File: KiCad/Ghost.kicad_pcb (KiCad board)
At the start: 2 copper layers, 90.3 x 63 mm, 68 parts, among them P1 MOTOR, P2 SERVO, P3 START, P4 PWM, P5 RGB, Q1 MMBT3904, SW1 BTN1, U1 INA219, U10 GP2Y0E02B, U11 GP2Y0E02B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

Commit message: Started on Feature Tests in Arduino
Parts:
- removed the REF** at (111.3, 103.6)
- added REF**: 3mm_mounting_hole, NorBotKiCadFootprints:3mm_mounting_hole, F.Cu at (111.3, 103.6)
- added REF**: 3mm_mounting_hole, NorBotKiCadFootprints:3mm_mounting_hole, F.Cu at (181.0, 130.0)
- added REF**: 3mm_mounting_hole, NorBotKiCadFootprints:3mm_mounting_hole, F.Cu at (181.0, 74.7)
- added REF**: 3mm_mounting_hole, NorBotKiCadFootprints:3mm_mounting_hole, F.Cu at (163.6, 99.3)
- added REF**: 3mm_mounting_hole, NorBotKiCadFootprints:3mm_mounting_hole, F.Cu at (163.8, 108.6)
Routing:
- net /IRSensors/SD3: track 37.0 -> 39.7 mm
- net WIFI_RX: track 22.3 -> 24.1 mm
- net /IRSensors/SC3: track 39.5 -> 40.8 mm
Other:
- outline, holes or cut-outs redrawn

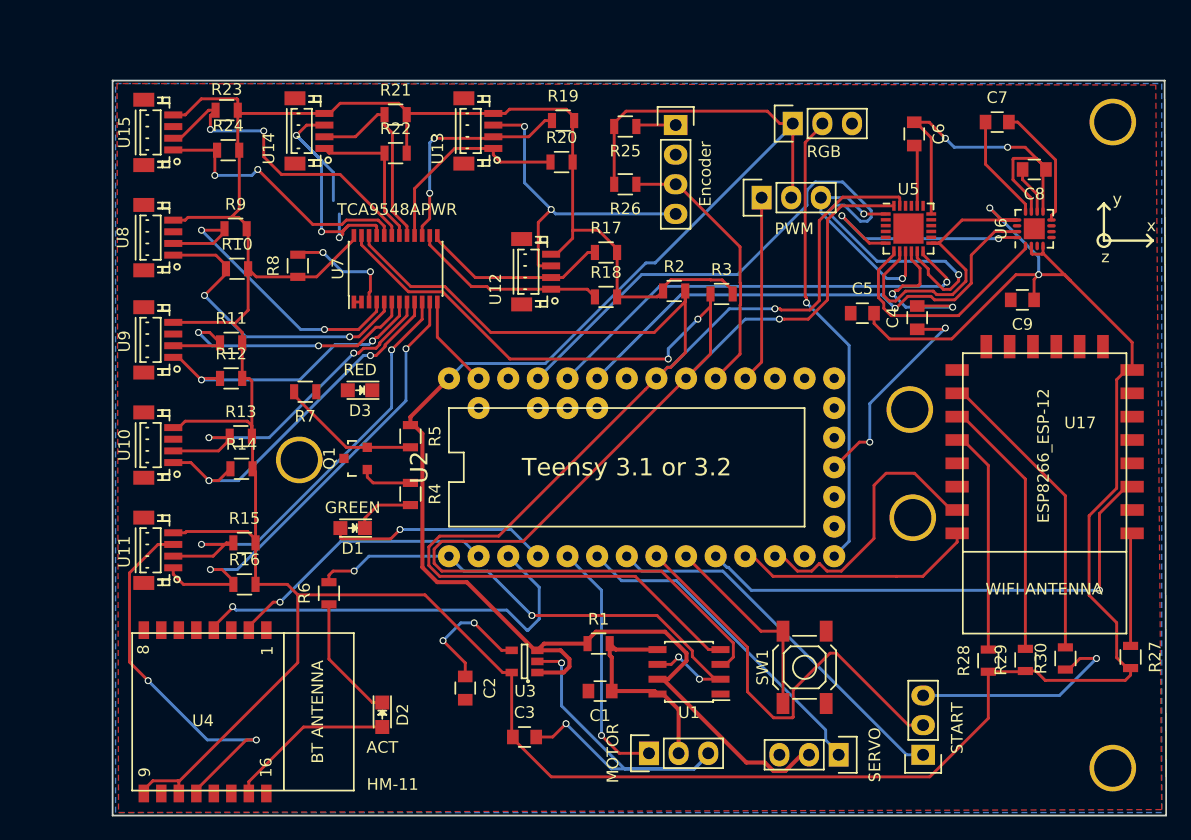
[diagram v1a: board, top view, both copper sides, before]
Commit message: Working on PCB layout for Rev 2
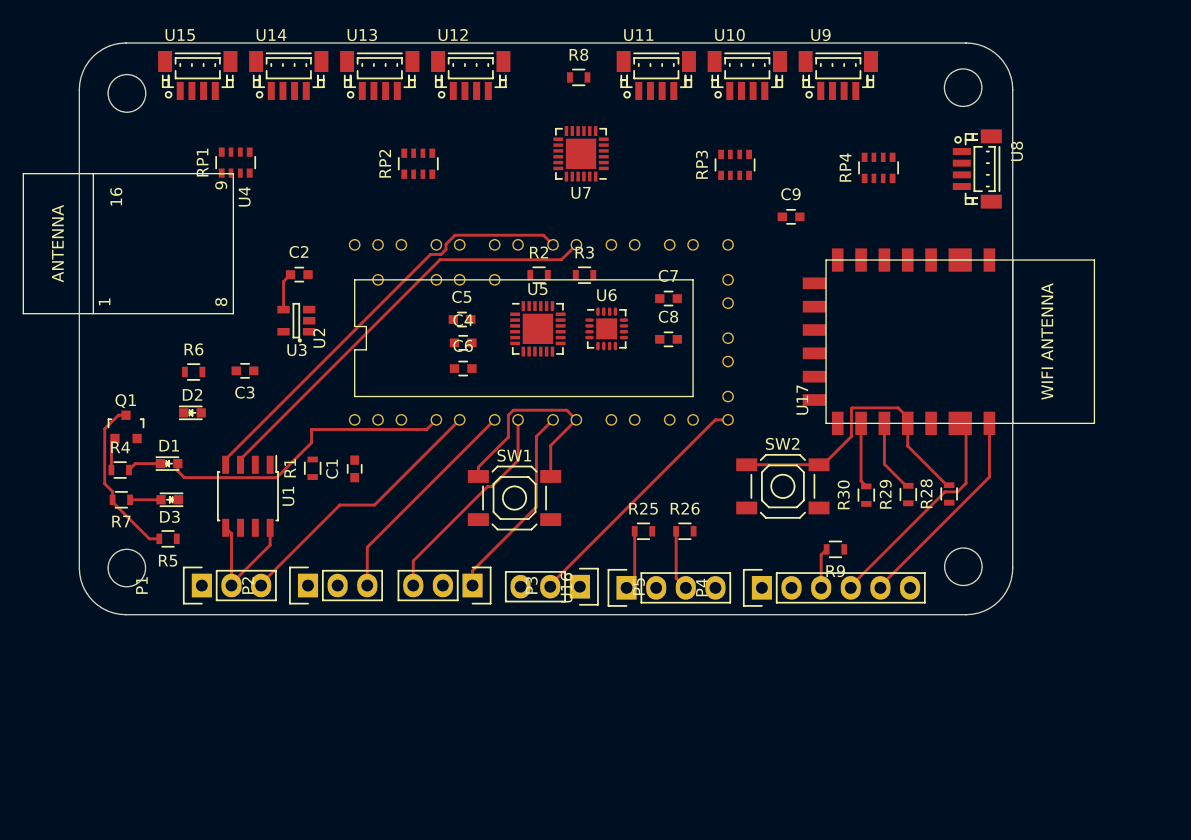
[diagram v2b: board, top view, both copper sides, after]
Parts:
- removed R10, R11, R12, R13, R14, R15, R16, R17, R18, R19, R20, R21, R22, R23, R24: 1k, Resistors_SMD:R_0805
- removed R27: 3k3, Resistors_SMD:R_0805
- removed REF**: Symbol_OSHW-Logo_SilkScreen, Symbols:Symbol_OSHW-Logo_SilkScreen
- removed REF** (x5): 3mm_mounting_hole, NorBotKiCadFootprints:3mm_mounting_hole
- added RP1: 4 x 1k ohm, Resistors_SMD:R_Array_Convex_4x0603, F.Cu at (105.8, 78.2)
- added RP2: 4 x 1k ohm, Resistors_SMD:R_Array_Convex_4x0603, F.Cu at (121.5, 78.2)
- added RP3: 4 x 1k ohm, Resistors_SMD:R_Array_Convex_4x0603, F.Cu at (148.6, 78.3)
- added RP4: 4 x 1k ohm, Resistors_SMD:R_Array_Convex_4x0603, F.Cu at (160.9, 78.6)
- added SW2: PROG, Buttons_Switches_SMD:SW_SPST_SKQG, F.Cu at (152.7, 105.9)
- C1, C2, C3, C4, C5, C6, C7, C8, C9: footprint Capacitors_SMD:C_0805 -> Capacitors_SMD:C_0603
- D1, D2, D3: footprint LEDs:LED_0805 -> LEDs:LED_0603
- P4: value PWM -> CONN_01X06; footprint Pin_Headers:Pin_Header_Straight_1x03 -> Pin_Headers:Pin_Header_Straight_1x06
- R1, R2, R25, R26, R28, R29, R3, R30, R4, R5, R6, R7, R8: footprint Resistors_SMD:R_0805 -> Resistors_SMD:R_0603
- R9: value 1k -> 0; footprint Resistors_SMD:R_0805 -> Resistors_SMD:R_0603
- U16: value Encoder -> Transmissive_Photo_Interrupter
- U2: value Teensy 3.1 or 3.2 -> Teensy31_32
- U7: value TCA9548APWR -> TCA9548ARGER; footprint Housings_SSOP:TSSOP-24_4.4x7.8mm_Pitch0.65mm -> Housings_DFN_QFN:QFN-24-1EP_4x4mm_Pitch0.5mm
- moved U8 70.4 mm to (169.3, 78.7), turned to 270 degrees
- moved U9 62.5 mm to (157.4, 70.8), turned to 0 degrees
- moved U10 59.5 mm to (149.7, 70.8), turned to 0 degrees
- moved U11 58.9 mm to (141.8, 70.8), turned to 0 degrees
- moved R9 58.3 mm to (157.2, 111.3), turned to 180 degrees
- moved P2 47.7 mm to (112.0, 114.4), turned to 90 degrees
- moved P5 43.7 mm to (135.3, 114.5), turned to 270 degrees
- moved C6 43.6 mm to (125.3, 95.8), turned to 0 degrees
- moved U4 41.3 mm to (96.6, 85.1), turned to 90 degrees
- moved P3 41.3 mm to (126.1, 114.4), turned to 270 degrees
- moved P1 40.9 mm to (102.9, 114.4)
- moved U1 40.7 mm to (106.8, 106.8), turned to 270 degrees
- moved U16 39.9 mm to (139.3, 114.6), turned to 90 degrees
- moved C3 39.5 mm to (106.6, 96.0), turned to 180 degrees
- moved C4 39.0 mm to (125.3, 93.6), turned to 0 degrees
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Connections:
- C9 pad 1: +3V3 -> GND
- C9 pad 2: GND -> +3V3
- P1 pad 1: MOTOR -> GND
- P1 pad 3: GND -> MOTOR
- P2 pad 1: STEERING -> GND
- P2 pad 3: GND -> STEERING
- P3 pad 1: START -> START_POWER
- P3 pad 2: START_POWER -> GND
- P3 pad 3: GND -> START
- P4 pad 1: PWM -> GND
- P4 pad 2: +5V -> (no net)
- P4 pad 3: GND -> Net-(P4-Pad3)
- P5 pad 1: +5V -> GND
- P5 pad 3: GND -> +5V
- Q1 pad 2: Net-(Q1-Pad2) -> GND
- Q1 pad 3: GND -> Net-(Q1-Pad3)
- R5 pad 2: Net-(Q1-Pad2) -> Net-(Q1-Pad3)
- R7 pad 2: Net-(Q1-Pad2) -> Net-(Q1-Pad3)
- R9 pad 1: /IRSensors/SD0 -> +5V
- R9 pad 2: +3V3 -> Net-(P4-Pad3)
- U10 pad 1: /IRSensors/SC2 -> /IRSensors/SCL_2
- U10 pad 2: /IRSensors/SD2 -> /IRSensors/SDA_2
- U11 pad 1: /IRSensors/SC3 -> /IRSensors/SCL_3
- U11 pad 2: /IRSensors/SD3 -> /IRSensors/SDA_3
- U12 pad 1: /IRSensors/SC4 -> /IRSensors/SCL_4
- U12 pad 2: /IRSensors/SD4 -> /IRSensors/SDA_4
- U13 pad 1: /IRSensors/SC5 -> /IRSensors/SCL_5
- U13 pad 2: /IRSensors/SD5 -> /IRSensors/SDA_5
- U14 pad 1: /IRSensors/SC6 -> /IRSensors/SCL_6
- U14 pad 2: /IRSensors/SD6 -> /IRSensors/SDA_6
- U15 pad 1: /IRSensors/SC7 -> /IRSensors/SCL_7
- U15 pad 2: /IRSensors/SD7 -> /IRSensors/SDA_7
- U17 pad 1: Net-(R27-Pad1) -> ~WIFI_RESET
- U2 pad 11: (no net) -> ~WIFI_RESET
- U2 pad 16: PWM -> (no net)
- U7 pad 1: GND -> /IRSensors/SDA_0
- U7 pad 10: /IRSensors/SD3 -> /IRSensors/SDA_4
- U7 pad 11: /IRSensors/SC3 -> /IRSensors/SCL_4
- U7 pad 12: GND -> /IRSensors/SDA_5
- U7 pad 13: /IRSensors/SD4 -> /IRSensors/SCL_5
- U7 pad 14: /IRSensors/SC4 -> /IRSensors/SDA_6
- U7 pad 15: /IRSensors/SD5 -> /IRSensors/SCL_6
- U7 pad 16: /IRSensors/SC5 -> /IRSensors/SDA_7
- U7 pad 17: /IRSensors/SD6 -> /IRSensors/SCL_7
- U7 pad 18: /IRSensors/SC6 -> GND
- U7 pad 19: /IRSensors/SD7 -> TEENSY_SCL
- U7 pad 2: GND -> /IRSensors/SCL_0
- U7 pad 20: /IRSensors/SC7 -> TEENSY_SDA
- U7 pad 21: GND -> +3V3
- U7 pad 22: TEENSY_SCL -> GND
- U7 pad 23: TEENSY_SDA -> GND
- U7 pad 24: +3V3 -> Net-(R8-Pad2)
- U7 pad 3: Net-(R8-Pad2) -> /IRSensors/SDA_1
- U7 pad 4: /IRSensors/SD0 -> /IRSensors/SCL_1
- U7 pad 5: /IRSensors/SC0 -> /IRSensors/SDA_2
- U7 pad 6: /IRSensors/SD1 -> /IRSensors/SCL_2
- U7 pad 7: /IRSensors/SC1 -> /IRSensors/SDA_3
- U7 pad 8: /IRSensors/SD2 -> /IRSensors/SCL_3
- U7 pad 9: /IRSensors/SC2 -> GND
- U8 pad 1: /IRSensors/SC0 -> /IRSensors/SCL_0
- U8 pad 2: /IRSensors/SD0 -> /IRSensors/SDA_0
- U9 pad 1: /IRSensors/SC1 -> /IRSensors/SCL_1
- U9 pad 2: /IRSensors/SD1 -> /IRSensors/SDA_1
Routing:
- net +3V3: track 375.1 -> 0.00 mm, vias 2 -> 0
- net GND: track 273.4 -> 0.00 mm, vias 20 -> 0
- net +5V: track 139.0 -> 0.00 mm
- net TEENSY_SDA: track 134.2 -> 36.9 mm, vias 3 -> 0
- net TEENSY_SCL: track 128.9 -> 37.1 mm, vias 1 -> 0
- net IMU_FSYNC: track 62.3 -> 0.00 mm, vias 1 -> 0
- net WIFI_ENABLE: track 44.4 -> 0.00 mm, vias 1 -> 0
- net IMU_DRDY: track 43.8 -> 0.00 mm, vias 1 -> 0
- net /IRSensors/SC3: track 40.8 -> 0.00 mm, vias 2 -> 0
- net /IRSensors/SD3: track 39.7 -> 0.00 mm, vias 2 -> 0
- net IMU_INT: track 39.4 -> 0.00 mm, vias 1 -> 0
- net BLUETOOTH_RX: track 36.7 -> 0.00 mm, vias 1 -> 0
- net /IRSensors/SC2: track 30.7 -> 0.00 mm, vias 2 -> 0
- net /IRSensors/SD2: track 29.9 -> 0.00 mm, vias 2 -> 0
- net /IRSensors/SD7: track 27.5 -> 0.00 mm, vias 2 -> 0
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- removed copper zone on B.Cu, net GND
- removed copper zone on F.Cu, net GND
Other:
- board size 90.3 x 63 mm -> 80 x 49 mm
- net class Power removed
- rule pad_to_mask_clearance: 0.2 -> 0
- board text removed: "Frode Lillerud, NorBot 20.june 2016"
- board text removed: "x"
- board text removed: "y"
- board text removed: "z"
